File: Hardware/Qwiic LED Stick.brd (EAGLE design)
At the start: 91.4 x 25.4 mm, 68 parts, among them J2 SMD, J3 PTH, J4 SMD, J6 AVR_SPI_PROG_3X2TESTPOINTS, U1 Tiny85-20-SMT

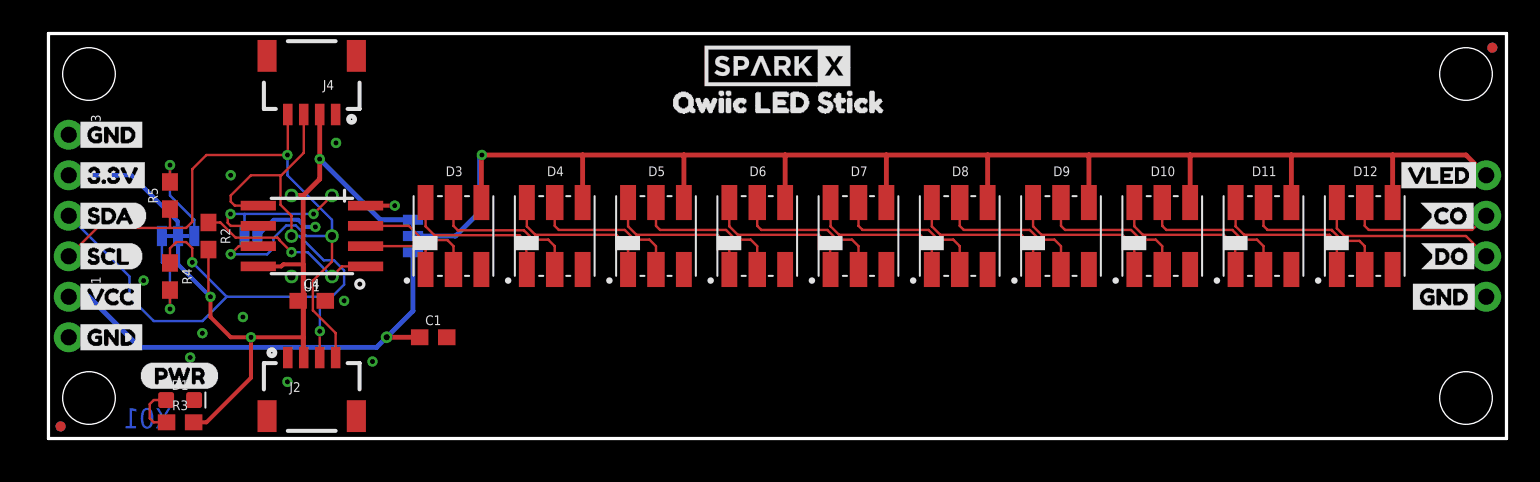
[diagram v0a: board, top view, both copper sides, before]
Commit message: Update schematic and board for transition
Brought schematic and board routing up to current standards
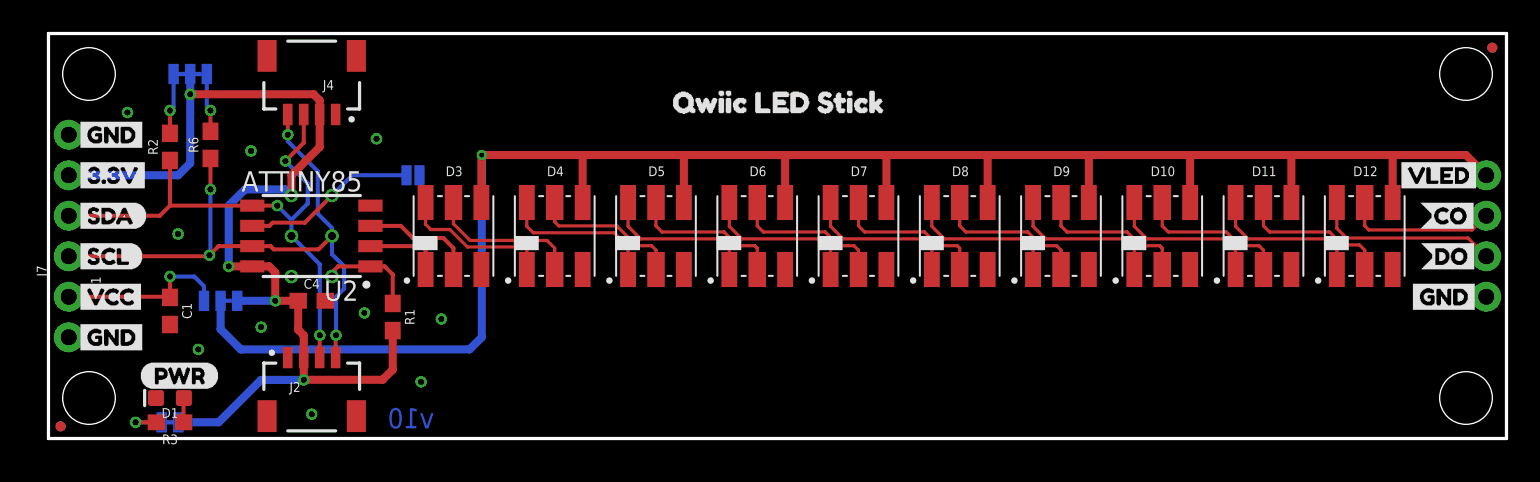
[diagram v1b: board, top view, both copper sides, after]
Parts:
- removed J3: PTH, SparkX:1X04_NO_SILK
- removed JP9: JUMPER-SMT_2_NO_SILK, SparkFun-Jumpers:SMT-JUMPER_2_NO_SILK
- removed R4, R5: 2.2k, SparkFun-Resistors:0603
- removed U$1, U$2: SPARKX-LOGO4, SparkX:SPARKX-MEDIUM
- removed U$29: (no value), Labels:QWIIC-LOGO-MEDIUM
- removed U1: Tiny85-20-SMT, Qwiic-Bluetooth-HC1x:SO08-EIAJ_MCU
- added ADDR: JUMPER-SMT_2_NO_SILK, SparkFun-Jumpers:SMT-JUMPER_2_NO_SILK
- added J7: (no value), SparkFun-Connectors:1X04_NO_SILK
- added LED: JUMPER-SMT_2_NC_TRACE_SILK, SparkFun-Jumpers:SMT-JUMPER_2_NC_TRACE_SILK
- added R1, R6: 4.7k, SparkFun-Resistors:0603
- added U2: ATTINY85, SparkFun-IC-Microcontroller:ATTINY85
- D10, D11, D12, D3, D4, D5, D6, D7, D8, D9: value APA1025050 -> APA102-5050
- I2C: value (none) -> JUMPER-SMT_3_2-NC_TRACE_SILK
- J2, J4: value SMD -> QWIIC_RA; device SparkX:1X04_1MM_RA -> SparkFun-Connectors:JST04_1MM_RA
- JP1, JP2, JP5, JP6: device SparkFun:MICRO-FIDUCIAL -> SparkFun-Aesthetics:FIDUCIAL-MICRO
- JP10: value (none) -> JUMPER-SMT_3_1-NC_TRACE_SILK
- JP3, JP4, JP7, JP8: device SparkFun:STAND-OFF -> SparkFun-Hardware:STAND-OFF
- moved C1 16.6 mm to (7.62, 8.00), turned to 270 degrees
- moved JP10 12.7 mm to (10.8, 8.64), turned to 180 degrees
- moved I2C 10.2 mm to (8.89, 22.9)
- moved R2 6.09 mm to (7.62, 18.3), turned to 90 degrees
- moved D1 0.65 mm to (7.62, 2.54), turned to 180 degrees
- moved R3 0.64 mm to (7.62, 1.02), turned to 180 degrees
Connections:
- removed net ADDR(MISO): J6.1, JP9.2, U1.6
- removed net N$1: I2C.1, R5.2
- removed net N$2: I2C.3, R4.2
- removed net SCL: J2.4, J3.4, J4.4, J6.3, R5.1, U1.7
- removed net SDA: J2.3, J3.3, J4.3, J6.4, R4.1, U1.5
- new net ADDR/CIPO: ADDR.2, J6.1, U2.6
- new net N$4: LED.1, R3.2
- new net N$5: I2C.3, R2.2
- new net N$6: I2C.1, R6.2
- new net SCL/SCK: J2.4, J4.4, J6.3, J7.1, R6.1, U2.7
- new net SDA/COPI: J2.3, J4.3, J6.4, J7.2, R2.1, U2.5
- net !RST: now also R1.1, U2.1; no longer R2.1, U1.1
- net 3.3V: now also J7.3, LED.2, R1.2, U2.8; no longer J3.2, R2.2, R3.2, U1.8
- net CLK: now also U2.3; no longer U1.3
- net DO: now also U2.2; no longer U1.2
- net GND: now also ADDR.1, J7.4, U2.4; no longer J3.1, JP9.1, U1.4
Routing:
- net SDA: track 51.6 -> 0.00 mm, vias 2 -> 0
- net SCL: track 46.6 -> 0.00 mm, vias 2 -> 0
- net SCL/SCK: track 0.00 -> 40.2 mm, vias 0 -> 4
- net SDA/COPI: track 0.00 -> 34.9 mm, vias 0 -> 3
- net VLED: track 101.9 -> 123.8 mm
- net VCC: track 29.6 -> 11.0 mm
- net ADDR/CIPO: track 0.00 -> 11.0 mm
- net ADDR(MISO): track 10.9 -> 0.00 mm, vias 2 -> 0
- net N$1: track 6.13 -> 0.00 mm, vias 1 -> 0
- net GND: track 6.07 -> 0.00 mm, vias 11 -> 10
- net N$2: track 5.96 -> 0.00 mm, vias 1 -> 0
- net !RST: track 11.5 -> 6.25 mm, vias 1 -> 0
- net N$5: track 0.00 -> 3.82 mm, vias 0 -> 1
- net N$6: track 0.00 -> 3.69 mm, vias 0 -> 1
- net N$4: track 0.00 -> 2.95 mm, vias 0 -> 1
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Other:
- board text added: "Revised by: Priyanka Makin"
- board text added: "v10"
- board text removed: "X01"
